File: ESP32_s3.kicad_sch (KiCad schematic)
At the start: 67 parts, among them J1 54-00127, J11 backup, J14 TXRX, J15 TXRX2, J3 Conn_01x02, J4 Servo motor, J6 jetson nano, J7 Conn_01x02, J8 Conn_01x02, J9 Conn_01x02, Q1 BSS138, SW1 SW_Push, SW2 SW_Push, U1 ESP32-S3-WROOM-1-N8R2, U2 LM1117T-ADJ, U3 L298N, U4 TPS61088RHLR

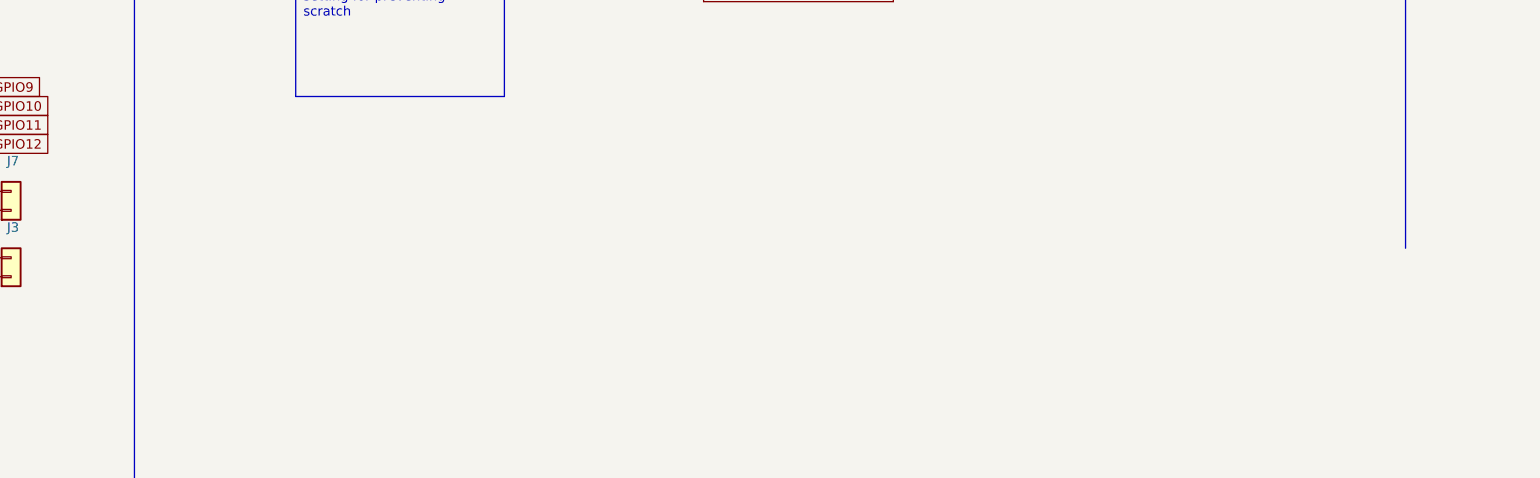
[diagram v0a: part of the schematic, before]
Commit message: update layout & mounting holes
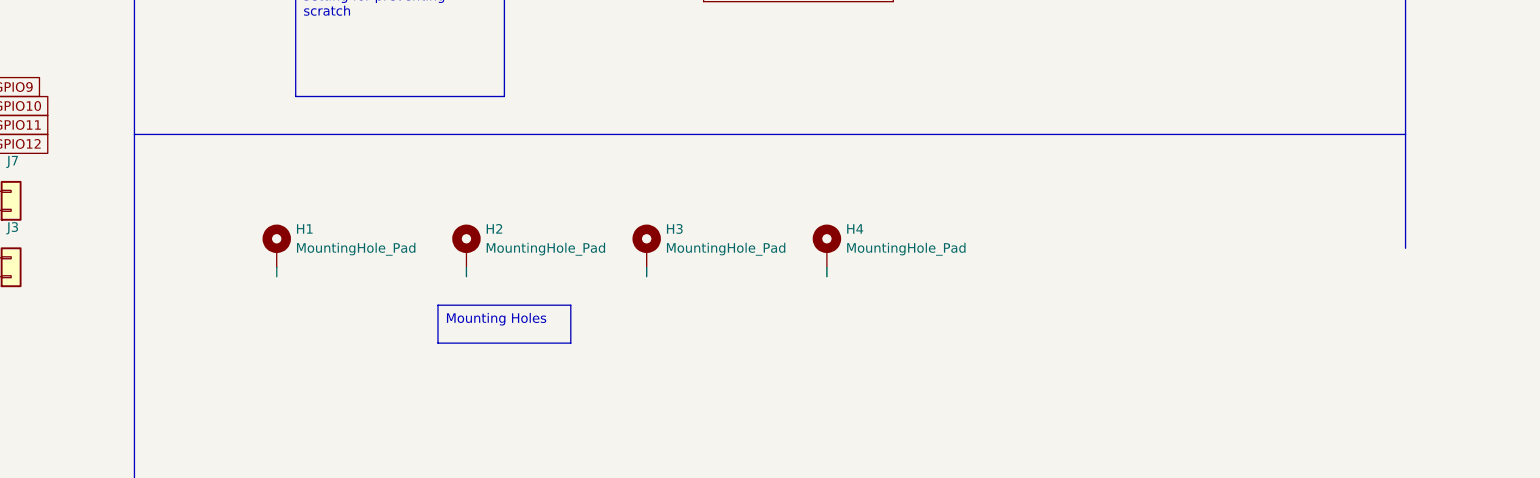
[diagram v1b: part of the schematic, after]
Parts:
- added H1, H2, H3, H4: MountingHole_Pad, MountingHole:MountingHole_3.2mm_M3_Pad_Via, symbol Mechanical:MountingHole_Pad

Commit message: update PCB layout
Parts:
- removed H1, H2, H3, H4: MountingHole_Pad, MountingHole:MountingHole_3.2mm_M3_Pad_Via, symbol Mechanical:MountingHole_Pad
- removed J6: jetson nano, 01x02connector:CONN_61300211121_WRE, symbol Connector:Conn_01x02_Pin
- removed R7: 16, CRGCQ0805F220R:RESC2012X65N, symbol Device:R_US
- added H1, H2, H3, H4: MountingHole, MountingHole:MountingHole_2.7mm, symbol Mechanical:MountingHole
- added NT1: NetTie_2, nettist:NetTie-2_SMD_Pad2.0mm, symbol Device:NetTie_2
- added R2: 16, CRGCQ0805F220R:RESC2012X65N, symbol Device:R_US
- L1: footprint MLZ2012M1R0HT000:INDC2012X145N -> VLP8040T_1R0N:IND_VLP8040T-1R0N_TDK
- U4: footprint TPS61088RHLR:RHL0020A -> TPS61088RHLR:IC_TPS61088RHLR
- renumbered D6 to D4, D7 to D5, D4 to D6, D5 to D7
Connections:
- net +5V: no longer J3.2 (Pin_2), J7.2 (Pin_2)
- net 3.3V: now also J3.2 (Pin_2), J7.2 (Pin_2)
- net GND: now also NT1.2, R2.1; no longer C7.2, Ccomp1.2, Ccomp2.2, Cin1.2, Cin2.2, Cout1.2, Css1.2, Cvcc1.2, D3.2 (A), D5.2 (A), D7.2 (A), D9.2 (A), DbLED1.1 (K), DrLED1.1 (K), Rfbb1.2, Rlim1.2, U3.1 (SENSE_A), U3.8 (GND), U4.11 (NC), U4.12 (NC), U4.20 (AGND), U4.21 (PGND)
- net GPIO10: now also U3.5 (IN1); no longer U3.7 (IN2)
- net GPIO11: no longer U3.10 (IN3)
- net GPIO12: no longer U3.12 (IN4)
- net GPIO20: now also LD2.2 (A)
- net GPIO3: now also U3.10 (IN3)
- net GPIO35: now also J11.2 (Pin_2)
- net GPIO36: now also J11.1 (Pin_1)
- net GPIO38: no longer LD2.2 (A)
- net GPIO41: no longer J11.1 (Pin_1)
- net GPIO42: no longer J11.2 (Pin_2)
- net GPIO46: now also U3.12 (IN4)
- net GPIO9: now also U3.7 (IN2); no longer U3.5 (IN1)
- net at LD2.1 (K): now also R2.2
- net INPUT V: now reaches CR1.2, J1.A
- new net PGND: C7.2, Ccomp1.2, Ccomp2.2, Cin1.2, Cin2.2, Cout1.2, Css1.2, Cvcc1.2, D3.2 (A), D5.2 (A), D7.2 (A), D9.2 (A), DbLED1.1 (K), DrLED1.1 (K), NT1.1, Rfbb1.2, Rlim1.2, U3.1 (SENSE_A), U3.8 (GND), U4.11 (NC), U4.12 (NC), U4.20 (AGND), U4.21 (PGND)
- no-connect marks 28 -> 24

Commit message: update PCB layout
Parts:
- removed CR1: SMAJ10A, SMAJ10A:SMASeries_LTF, symbol 2024-10-10_19-12-55:SMAJ10A
- added CR1: SMAJ5.0A, SMASeries_LTF, symbol 2024-10-15_18-29-22:SMAJ5.0A
- added U5, U6, U7, U8: BAT54, SOT-23_3L_ONS, symbol 2024-10-15_19-32-28:BAT54
- L1: footprint VLP8040T_1R0N:IND_VLP8040T-1R0N_TDK -> VLS6045EX_1R0N:IND_VLS6045EX-1R0N
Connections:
- net +5V: now also CR1.1
- net GPIO1: now also U5.1; no longer J14.2 (Pin_2)
- net GPIO2: now also U6.1; no longer J14.1 (Pin_1)
- net INPUT V: now also CR1.2
- net RXD0: now also U8.1; no longer J15.1 (Pin_1)
- net TXD0: now also U7.1; no longer J15.2 (Pin_2)
- new net: J15.2 (Pin_2), U7.3
- new net: J14.2 (Pin_2), U5.3
- new net: J14.1 (Pin_1), U6.3
- new net: J15.1 (Pin_1), U8.3
- no-connect marks 24 -> 28
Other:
- moved on the sheet: H1, H2, H3, H4

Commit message: update PCB
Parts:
- removed CR1: SMAJ5.0A, SMASeries_LTF, symbol 2024-10-15_18-29-22:SMAJ5.0A
- removed U5, U6, U7, U8: BAT54, SOT-23_3L_ONS, symbol 2024-10-15_19-32-28:BAT54
- added CR1: SMAJ10A, SMAJ10A:SMASeries_LTF, symbol 2024-10-10_19-12-55:SMAJ10A
- added J2: 54-00127, 54_00127:TENSILITY_54-00127, symbol 54-00127:54-00127
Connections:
- net +5V: now also CR1.1
- net GPIO1: now also J14.2 (Pin_2)
- net GPIO2: now also J14.1 (Pin_1)
- net INPUT V: now also CR1.2
- net RXD0: now also J15.1 (Pin_1)
- net TXD0: now also J15.2 (Pin_2)
- no-connect marks 28 -> 24
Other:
- moved on the sheet: H1, H2, H3, H4

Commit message: update PCB
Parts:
- CR1: footprint SMAJ10A:SMASeries_LTF -> footprints:SMASeries_LTF
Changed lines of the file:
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@@
 			)
 		)
-		(property "Footprint" "SMAJ10A:SMASeries_LTF"
+		(property "Footprint" "footprints:SMASeries_LTF"
 			(at 74.93 49.53 0)
 			(effects

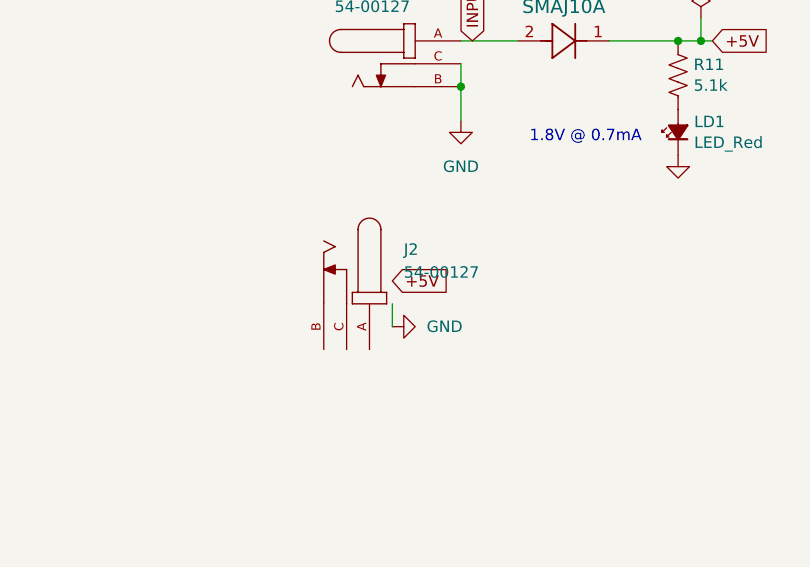
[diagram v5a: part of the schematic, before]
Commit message: remove jetson power and fix acute angle
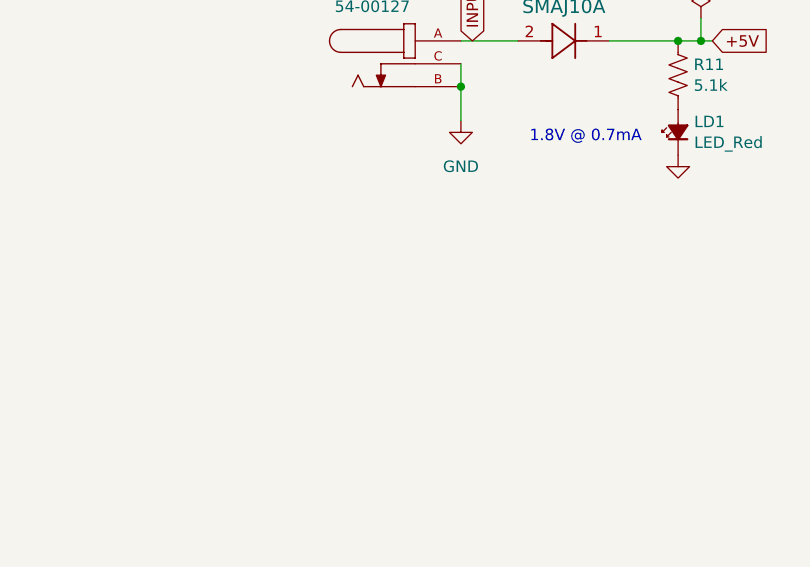
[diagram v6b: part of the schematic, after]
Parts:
- removed J2: 54-00127, 54_00127:TENSILITY_54-00127, symbol 54-00127:54-00127
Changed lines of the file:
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@@
 	(wire
 		(pts
-			(xy 60.96 78.74) (xy 60.96 81.28)
-		)
-		(stroke
-			(width 0)
-			(type default)
-		)
-	)
-	(wire
-		(pts
 			(xy 95.25 49.53) (xy 92.71 49.53)
 		)
@@
 		)
 	)
-	(global_label "+5V"
-		(shape input)
-		(at 60.96 76.2 0)
-		(fields_autoplaced yes)
-		(effects
-			(font
-				(size 1.27 1.27)
-			)
-			(justify left)
-		)
-		(property "Intersheetrefs" "${INTERSHEET_REFS}"
-			(at 67.8157 76.2 0)
-			(effects
-				(font
-					(size 1.27 1.27)
-				)
-				(justify left)
-				(hide yes)
-			)
-		)
-	)
 	(global_label "GPIO10"
 		(shape input)
@@
 	)
 	(symbol
-		(lib_id "54-00127:54-00127")
-		(at 55.88 78.74 270)
-		(unit 1)
-		(exclude_from_sim no)
-		(in_bom yes)
-		(on_board yes)
-		(dnp no)
-		(fields_autoplaced yes)
-		(property "Reference" "J2"
-			(at 62.23 72.7102 90)
-			(effects
-				(font
-					(size 1.27 1.27)
-				)
-				(justify left)
-			)
-		)
-		(property "Value" "54-00127"
-			(at 62.23 75.2502 90)
-			(effects
-				(font
-					(size 1.27 1.27)
-				)
-				(justify left)
-			)
-		)
-		(property "Footprint" "54_00127:TENSILITY_54-00127"
-			(at 55.88 78.74 0)
-			(effects
-				(font
-					(size 1.27 1.27)
-				)
-				(justify bottom)
-				(hide yes)
-			)
-		)
-		(property "Datasheet" "https://www.snapeda.com/parts/54-00127/Tensility%20International%20Corp/datasheet/"
-			(at 55.88 78.74 0)
-			(effects
-				(font
-					(size 1.27 1.27)
-				)
-				(hide yes)
-			)
-		)
-		(property "Description" ""
-			(at 55.88 78.74 0)
-			(effects
-				(font
-					(size 1.27 1.27)
-				)
-				(hide yes)
-			)
-		)
-		(property "PARTREV" "A"
-			(at 55.88 78.74 0)
-			(effects
-				(font
-					(size 1.27 1.27)
-				)
-				(justify bottom)
-				(hide yes)
-			)
-		)
-		(property "STANDARD" "Manufacturer Recommendations"
-			(at 55.88 78.74 0)
-			(effects
-				(font
-					(size 1.27 1.27)
-				)
-				(justify bottom)
-				(hide yes)
-			)
-		)
-		(property "SNAPEDA_PN" "54-00127"
-			(at 55.88 78.74 0)
-			(effects
-				(font
-					(size 1.27 1.27)
-				)
-				(justify bottom)
-				(hide yes)
-			)
-		)
-		(property "MAXIMUM_PACKAGE_HEIGHT" "7.3mm"
-			(at 55.88 78.74 0)
-			(effects
-				(font
-					(size 1.27 1.27)
-				)
-				(justify bottom)
-				(hide yes)
-			)
-		)
-		(property "MANUFACTURER" "TENSILITY"
-			(at 55.88 78.74 0)
-			(effects
-				(font
-					(size 1.27 1.27)
-				)
-				(justify bottom)
-				(hide yes)
-			)
-		)
-		(pin "C"
-		)
-		(pin "A"
-		)
-		(pin "B"
-		)
-		(instances
-			(project "ESP32_s3"
-				(path "/17b1a26b-4dd3-45da-ac9f-9f7d4372170f"
-					(reference "J2")
-					(unit 1)
-				)
-			)
-		)
-	)
-	(symbol
 		(lib_id "Device:C")
 		(at 270.51 44.45 0)
@@
 					(unit 1)
 				)
-			)
-		)
-	)
-	(symbol
-		(lib_id "power:GND")
-		(at 60.96 81.28 90)
-		(unit 1)
-		(exclude_from_sim no)
-		(in_bom yes)
-		(on_board yes)
-		(dnp no)
-		(fields_autoplaced yes)
-		(property "Reference" "#PWR02"
-			(at 67.31 81.28 0)
-			(effects
-				(font
-					(size 1.27 1.27)
-				)
-				(hide yes)
-			)
-		)
-		(property "Value" "GND"
-			(at 64.77 81.2799 90)
-			(effects
-				(font
-					(size 1.27 1.27)
-				)
-				(justify right)
-			)
-		)
-		(property "Footprint" ""
-			(at 60.96 81.28 0)
-			(effects
-				(font
-					(size 1.27 1.27)
-				)
-				(hide yes)
-			)
-		)
-		(property "Datasheet" ""
-			(at 60.96 81.28 0)
-			(effects
-				(font
-					(size 1.27 1.27)
-				)
-				(hide yes)
-			)
-		)
-		(property "Description" "Power symbol creates a global label with name \"GND\" , ground"
-			(at 60.96 81.28 0)
-			(effects
-				(font
-					(size 1.27 1.27)
-				)
-				(hide yes)
-			)
-		)
-		(pin "1"
-		)
-		(instances
-			(project "ESP32_s3"
-				(path "/17b1a26b-4dd3-45da-ac9f-9f7d4372170f"
-					(reference "#PWR02")
-					(unit 1)
-				)
